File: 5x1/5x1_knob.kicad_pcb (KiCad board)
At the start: 2 copper layers, 25.3 x 25.3 mm, 8 parts

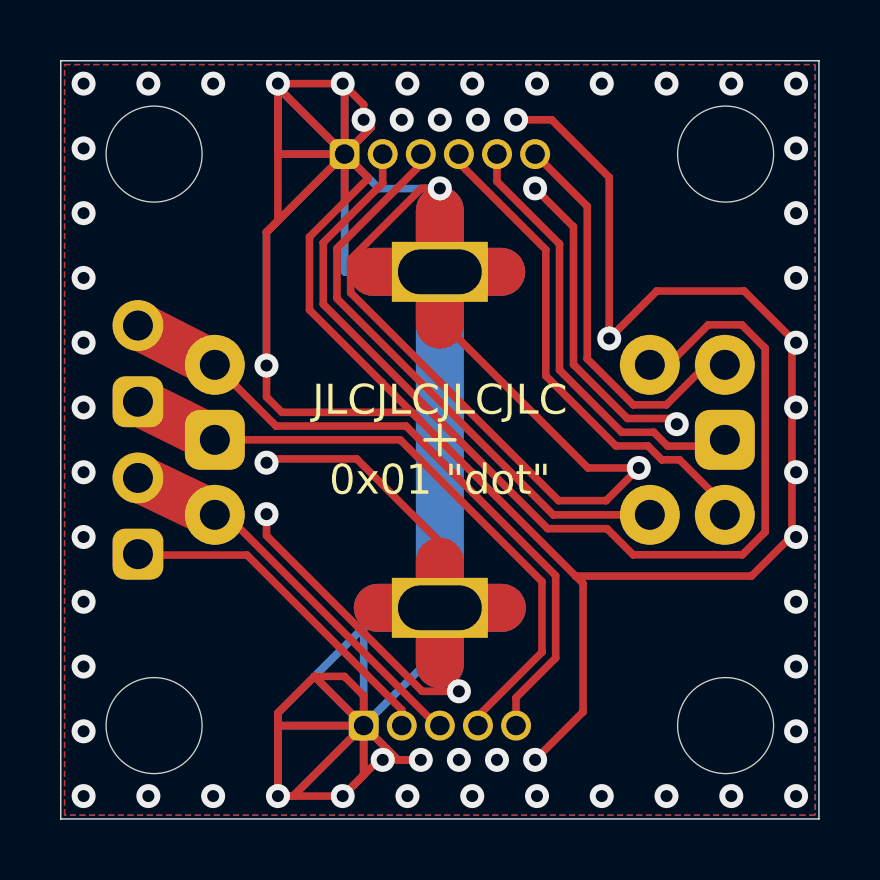
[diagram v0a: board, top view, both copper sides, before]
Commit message: touched up things and detached the case ground and electrical ground on the dot board
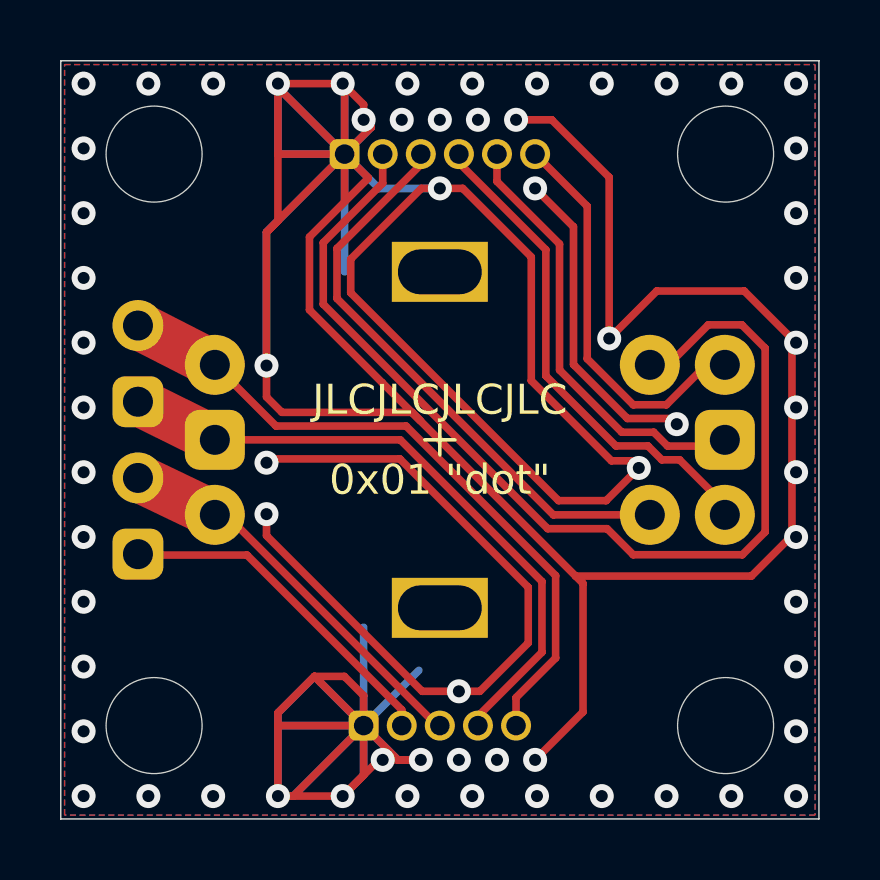
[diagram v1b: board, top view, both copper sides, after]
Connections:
- SW_1 pad MP: K_GND -> (no net)
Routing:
- net K_GND: track 276.0 -> 236.6 mm
